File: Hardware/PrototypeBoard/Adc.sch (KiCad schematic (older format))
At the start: 25 parts

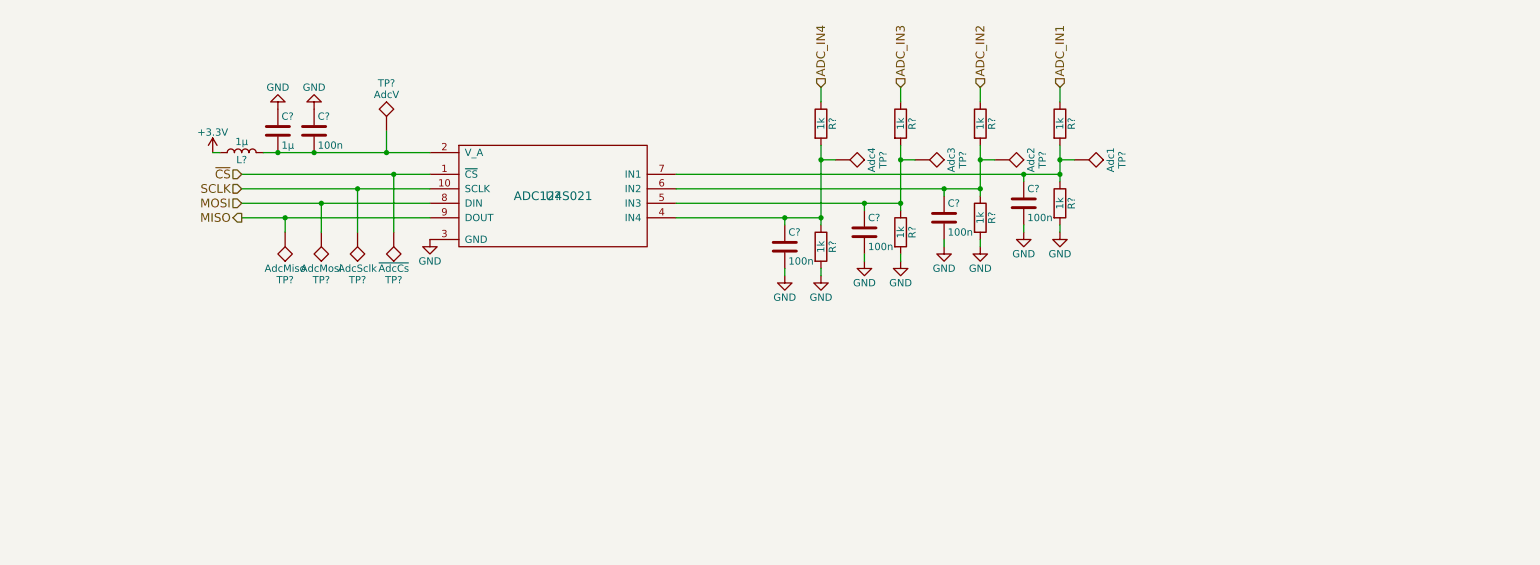
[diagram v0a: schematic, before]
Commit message: Fixed all ERC errors. Added power consumption estimation and other comments. Added links to datasheets. Dimensioned low pass and voltage dividers. Added TVS diodes for protection of voltage rails and ADC inputs. Added fuses. Added Testpoints. Added DC-link capacitors.
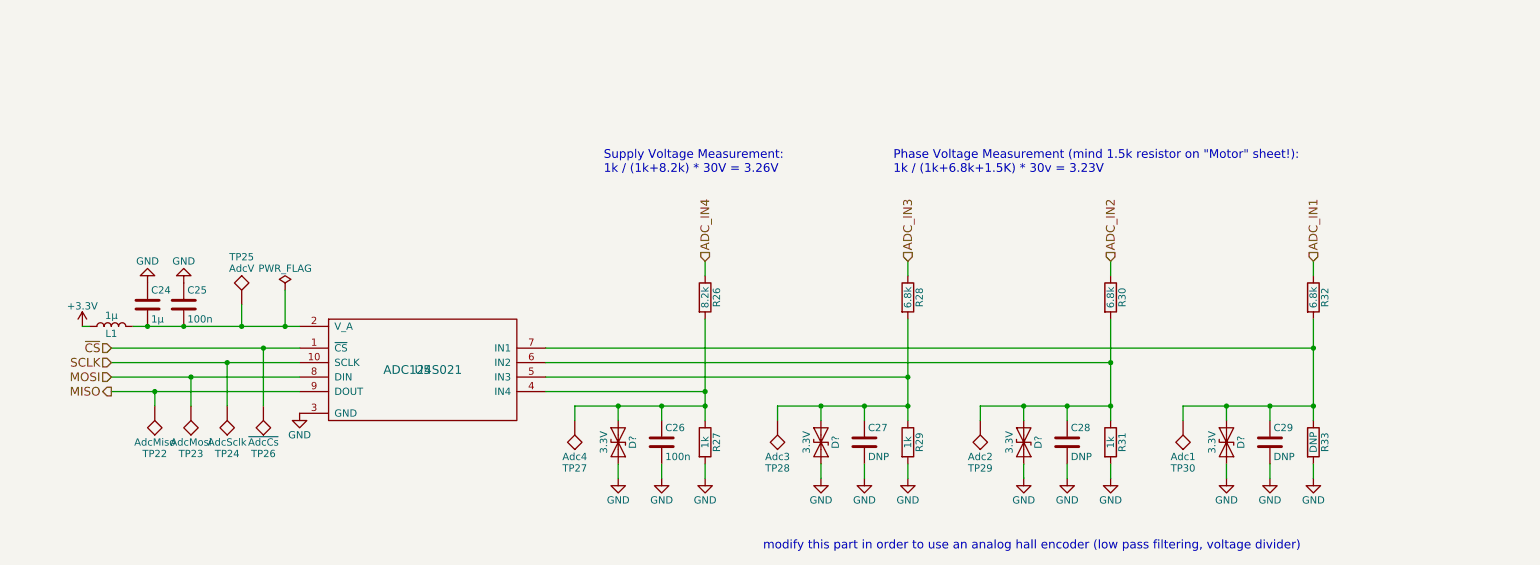
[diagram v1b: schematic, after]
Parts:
- added D? (x4): 3.3V, symbol D_TVS
- C27, C28, C29: renamed from C?; value 100n -> DNP
- R26: renamed from R?; value 1k -> 8.2k
- R28, R30, R32: renamed from R?; value 1k -> 6.8k
- R33: renamed from R?; value 1k -> DNP
- gave numbers to parts that had none: 17
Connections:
- net GND: now also D?.2 (A2), D?.2 (A2), D?.2 (A2), D?.2 (A2)
- net at C26.1, R26.2, R27.1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: now also D?.1 (A1)
- net at C27.1, R28.2, R29.1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: now also D?.1 (A1)
- net at C28.1, R30.2, R31.1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: now also D?.1 (A1)
- net at C29.1, R32.2, R33.1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: now also D?.1 (A1)
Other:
- note added: "Phase Voltage Measurement (mind 1.5k resistor on "Motor" sheet!):\n1k / (1k+6.8k+1.5K) * 30v = 3.23V"
- note added: "Supply Voltage Measurement:\n1k / (1k+8.2k) * 30V = 3.26V"
- note added: "modify this part in order to use an analog hall encoder (low pass filtering, voltage divider)"
- moved on the sheet: C24, C25, C26, C27, C28, C29, L1, R26, R27, R28, R29, R30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

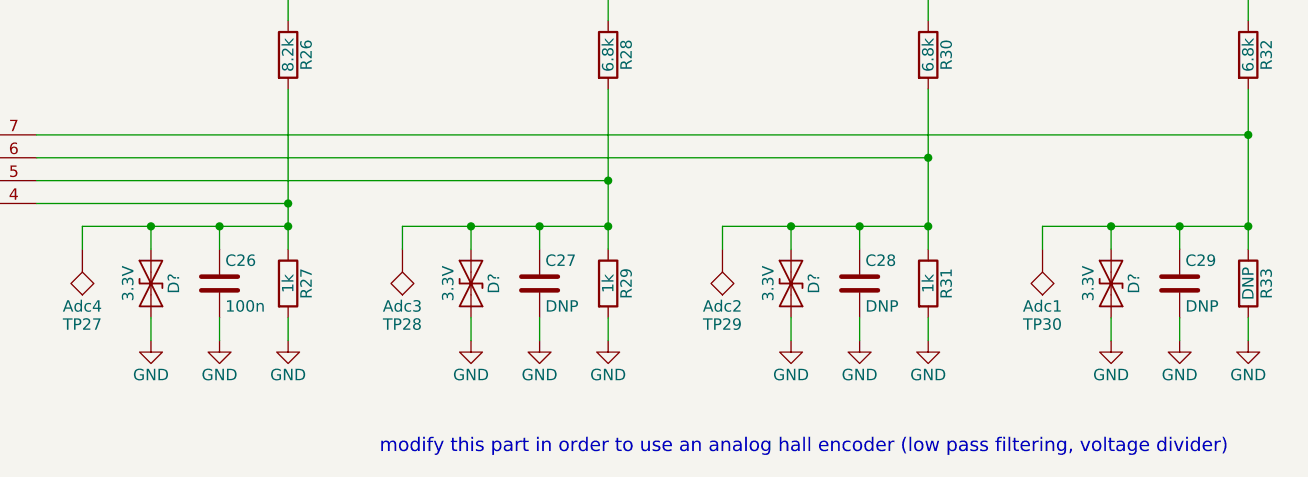
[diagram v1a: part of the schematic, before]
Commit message: Assigned footprints (some of them might still be incorrect). Added relative path to footprints. Generated Netlist.
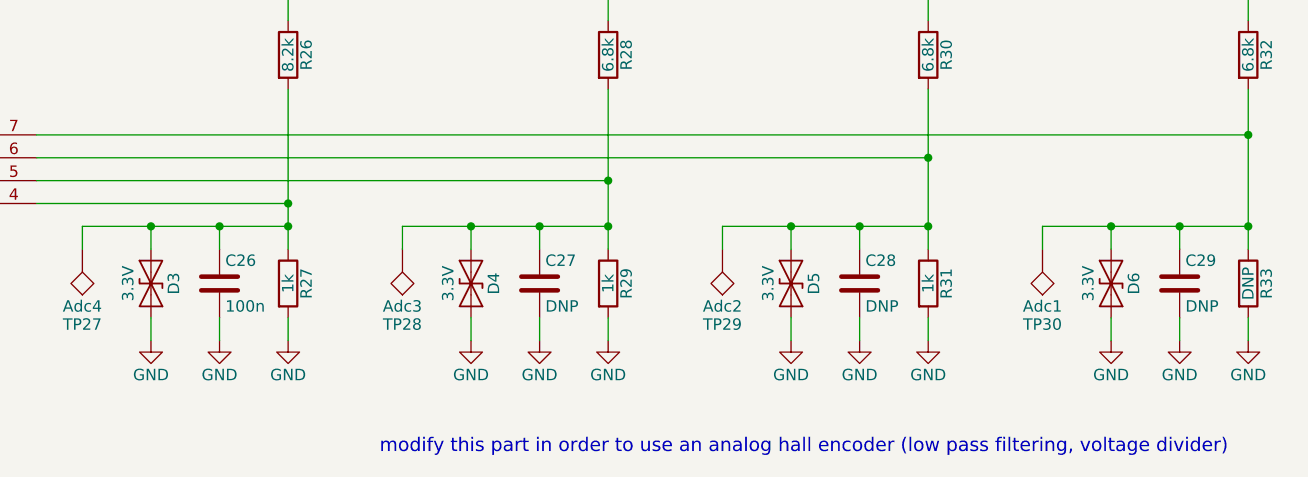
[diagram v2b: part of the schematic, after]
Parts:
- C24, C25, C26, C27, C28, C29: footprint (none) -> Capacitors_SMD:C_0805_HandSoldering
- D3, D4, D5, D6: renamed from D?; footprint (none) -> Diodes_SMD:D_SOD-323_HandSoldering
- L1: footprint (none) -> Inductors_SMD:L_0805_HandSoldering
- R26, R27, R28, R29, R30, R31, R32, R33: footprint (none) -> Resistors_SMD:R_0805_HandSoldering
- TP22, TP23, TP24, TP25, TP26, TP27, TP28, TP29, TP30: footprint (none) -> Measurement_Points:Measurement_Point_Round-TH_Big
- U5: footprint (none) -> libs:ADC124S021CIMMXNOPB
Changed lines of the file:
@@
 F 0 "U5" H 4050 3550 60  0000 C CNN
 F 1 "ADC124S021" H 4050 3550 60  0000 C CNN
-F 2 "" H 4050 3550 60  0001 C CNN
+F 2 "libs:ADC124S021CIMMXNOPB" H 4050 3550 60  0001 C CNN
 F 3 "" H 4050 3550 60  0001 C CNN
 	1    4050 3550
@@
 F 0 "L1" V 1850 3250 50  0000 C CNN
 F 1 "1μ" V 1975 3250 50  0000 C CNN
-F 2 "" H 1900 3250 50  0001 C CNN
+F 2 "Inductors_SMD:L_0805_HandSoldering" H 1900 3250 50  0001 C CNN
 F 3 "" H 1900 3250 50  0001 C CNN
 	1    1900 3250
@@
 F 0 "C25" H 2425 3200 50  0000 L CNN
 F 1 "100n" H 2425 3000 50  0000 L CNN
-F 2 "" H 2438 2950 50  0001 C CNN
+F 2 "Capacitors_SMD:C_0805_HandSoldering" H 2438 2950 50  0001 C CNN
 F 3 "" H 2400 3100 50  0001 C CNN
 	1    2400 3100
@@
 F 0 "C24" H 2175 3200 50  0000 L CNN
 F 1 "1μ" H 2175 3000 50  0000 L CNN
-F 2 "" H 2188 2950 50  0001 C CNN
+F 2 "Capacitors_SMD:C_0805_HandSoldering" H 2188 2950 50  0001 C CNN
 F 3 "" H 2150 3100 50  0001 C CNN
 	1    2150 3100
@@
 F 0 "C29" H 9925 4150 50  0000 L CNN
 F 1 "DNP" H 9925 3950 50  0000 L CNN
-F 2 "" H 9938 3900 50  0001 C CNN
+F 2 "Capacitors_SMD:C_0805_HandSoldering" H 9938 3900 50  0001 C CNN
 F 3 "" H 9900 4050 50  0001 C CNN
 	1    9900 4050
@@
 F 0 "C28" H 8525 4150 50  0000 L CNN
 F 1 "DNP" H 8525 3950 50  0000 L CNN
-F 2 "" H 8538 3900 50  0001 C CNN
+F 2 "Capacitors_SMD:C_0805_HandSoldering" H 8538 3900 50  0001 C CNN
 F 3 "" H 8500 4050 50  0001 C CNN
 	1    8500 4050
@@
 F 0 "C27" H 7125 4150 50  0000 L CNN
 F 1 "DNP" H 7125 3950 50  0000 L CNN
-F 2 "" H 7138 3900 50  0001 C CNN
+F 2 "Capacitors_SMD:C_0805_HandSoldering" H 7138 3900 50  0001 C CNN
 F 3 "" H 7100 4050 50  0001 C CNN
 	1    7100 4050
@@
 F 0 "C26" H 5725 4150 50  0000 L CNN
 F 1 "100n" H 5725 3950 50  0000 L CNN
-F 2 "" H 5738 3900 50  0001 C CNN
+F 2 "Capacitors_SMD:C_0805_HandSoldering" H 5738 3900 50  0001 C CNN
 F 3 "" H 5700 4050 50  0001 C CNN
 	1    5700 4050
@@
 F 0 "R26" V 6080 3050 50  0000 C CNN
 F 1 "8.2k" V 6000 3050 50  0000 C CNN
-F 2 "" V 5930 3050 50  0001 C CNN
+F 2 "Resistors_SMD:R_0805_HandSoldering" V 5930 3050 50  0001 C CNN
 F 3 "" H 6000 3050 50  0001 C CNN
 	1    6000 3050
@@
 F 0 "R28" V 7480 3050 50  0000 C CNN
 F 1 "6.8k" V 7400 3050 50  0000 C CNN
-F 2 "" V 7330 3050 50  0001 C CNN
+F 2 "Resistors_SMD:R_0805_HandSoldering" V 7330 3050 50  0001 C CNN
 F 3 "" H 7400 3050 50  0001 C CNN
 	1    7400 3050
@@
 F 0 "R30" V 8880 3050 50  0000 C CNN
 F 1 "6.8k" V 8800 3050 50  0000 C CNN
-F 2 "" V 8730 3050 50  0001 C CNN
+F 2 "Resistors_SMD:R_0805_HandSoldering" V 8730 3050 50  0001 C CNN
 F 3 "" H 8800 3050 50  0001 C CNN
 	1    8800 3050
@@
 F 0 "R32" V 10280 3050 50  0000 C CNN
 F 1 "6.8k" V 10200 3050 50  0000 C CNN
-F 2 "" V 10130 3050 50  0001 C CNN
+F 2 "Resistors_SMD:R_0805_HandSoldering" V 10130 3050 50  0001 C CNN
 F 3 "" H 10200 3050 50  0001 C CNN
 	1    10200 3050
@@
 F 0 "R33" V 10280 4050 50  0000 C CNN
 F 1 "DNP" V 10200 4050 50  0000 C CNN
-F 2 "" V 10130 4050 50  0001 C CNN
+F 2 "Resistors_SMD:R_0805_HandSoldering" V 10130 4050 50  0001 C CNN
 F 3 "" H 10200 4050 50  0001 C CNN
 	1    10200 4050
@@
 F 0 "R31" V 8880 4050 50  0000 C CNN
 F 1 "1k" V 8800 4050 50  0000 C CNN
-F 2 "" V 8730 4050 50  0001 C CNN
+F 2 "Resistors_SMD:R_0805_HandSoldering" V 8730 4050 50  0001 C CNN
 F 3 "" H 8800 4050 50  0001 C CNN
 	1    8800 4050
@@
 F 0 "R29" V 7480 4050 50  0000 C CNN
 F 1 "1k" V 7400 4050 50  0000 C CNN
-F 2 "" V 7330 4050 50  0001 C CNN
+F 2 "Resistors_SMD:R_0805_HandSoldering" V 7330 4050 50  0001 C CNN
 F 3 "" H 7400 4050 50  0001 C CNN
 	1    7400 4050
@@
 F 0 "R27" V 6080 4050 50  0000 C CNN
 F 1 "1k" V 6000 4050 50  0000 C CNN
-F 2 "" V 5930 4050 50  0001 C CNN
+F 2 "Resistors_SMD:R_0805_HandSoldering" V 5930 4050 50  0001 C CNN
 F 3 "" H 6000 4050 50  0001 C CNN
 	1    6000 4050
@@
 F 0 "TP27" H 5100 4200 50  0000 C BNN
 F 1 "Adc4" H 5100 4150 50  0000 C CNN
-F 2 "" H 5100 3900 50  0001 C CNN
+F 2 "Measurement_Points:Measurement_Point_Round-TH_Big" H 5100 3900 50  0001 C CNN
 F 3 "" H 5100 3900 50  0001 C CNN
 	1    5100 3900
@@
 F 0 "TP28" H 6500 4200 50  0000 C BNN
 F 1 "Adc3" H 6500 4150 50  0000 C CNN
-F 2 "" H 6500 3900 50  0001 C CNN
+F 2 "Measurement_Points:Measurement_Point_Round-TH_Big" H 6500 3900 50  0001 C CNN
 F 3 "" H 6500 3900 50  0001 C CNN
 	1    6500 3900
@@
 F 0 "TP29" H 7900 4200 50  0000 C BNN
 F 1 "Adc2" H 7900 4150 50  0000 C CNN
-F 2 "" H 7900 3900 50  0001 C CNN
+F 2 "Measurement_Points:Measurement_Point_Round-TH_Big" H 7900 3900 50  0001 C CNN
 F 3 "" H 7900 3900 50  0001 C CNN
 	1    7900 3900
@@
 F 0 "TP30" H 9300 4200 50  0000 C BNN
 F 1 "Adc1" H 9300 4150 50  0000 C CNN
-F 2 "" H 9300 3900 50  0001 C CNN
+F 2 "Measurement_Points:Measurement_Point_Round-TH_Big" H 9300 3900 50  0001 C CNN
 F 3 "" H 9300 3900 50  0001 C CNN
 	1    9300 3900
@@
 F 0 "TP25" H 2800 3400 50  0000 C BNN
 F 1 "AdcV" H 2800 3350 50  0000 C CNN
-F 2 "" H 2800 3100 50  0001 C CNN
+F 2 "Measurement_Points:Measurement_Point_Round-TH_Big" H 2800 3100 50  0001 C CNN
 F 3 "" H 2800 3100 50  0001 C CNN
 	1    2800 3100
@@
 F 0 "TP26" H 2950 4100 50  0000 C BNN
 F 1 "~AdcCs" H 2950 4050 50  0000 C CNN
-F 2 "" H 2950 3800 50  0001 C CNN
+F 2 "Measurement_Points:Measurement_Point_Round-TH_Big" H 2950 3800 50  0001 C CNN
 F 3 "" H 2950 3800 50  0001 C CNN
 	1    2950 3800
@@
 F 0 "TP24" H 2700 4100 50  0000 C BNN
 F 1 "AdcSclk" H 2700 4050 50  0000 C CNN
-F 2 "" H 2700 3800 50  0001 C CNN
+F 2 "Measurement_Points:Measurement_Point_Round-TH_Big" H 2700 3800 50  0001 C CNN
 F 3 "" H 2700 3800 50  0001 C CNN
 	1    2700 3800
@@
 F 0 "TP23" H 2450 4100 50  0000 C BNN
 F 1 "AdcMosi" H 2450 4050 50  0000 C CNN
-F 2 "" H 2450 3800 50  0001 C CNN
+F 2 "Measurement_Points:Measurement_Point_Round-TH_Big" H 2450 3800 50  0001 C CNN
 F 3 "" H 2450 3800 50  0001 C CNN
 	1    2450 3800
@@
 F 0 "TP22" H 2200 4100 50  0000 C BNN
 F 1 "AdcMiso" H 2200 4050 50  0000 C CNN
-F 2 "" H 2200 3800 50  0001 C CNN
+F 2 "Measurement_Points:Measurement_Point_Round-TH_Big" H 2200 3800 50  0001 C CNN
 F 3 "" H 2200 3800 50  0001 C CNN
 	1    2200 3800
@@
 modify this part in order to use an analog hall encoder (low pass filtering, voltage divider)
 $Comp
-L D_TVS D?
+L D_TVS D6
 U 1 1 5AFF1E54
 P 9600 4050
-F 0 "D?" H 9600 4150 50  0000 C CNN
+F 0 "D6" H 9600 4150 50  0000 C CNN
 F 1 "3.3V" H 9600 3950 50  0000 C CNN
-F 2 "" H 9600 4050 50  0001 C CNN
+F 2 "Diodes_SMD:D_SOD-323_HandSoldering" H 9600 4050 50  0001 C CNN
 F 3 "" H 9600 4050 50  0001 C CNN
 	1    9600 4050
@@
 $EndComp
 $Comp
-L D_TVS D?
+L D_TVS D3
 U 1 1 5AFF1F87
 P 5400 4050
-F 0 "D?" H 5400 4150 50  0000 C CNN
+F 0 "D3" H 5400 4150 50  0000 C CNN
 F 1 "3.3V" H 5400 3950 50  0000 C CNN
-F 2 "" H 5400 4050 50  0001 C CNN
+F 2 "Diodes_SMD:D_SOD-323_HandSoldering" H 5400 4050 50  0001 C CNN
 F 3 "" H 5400 4050 50  0001 C CNN
 	1    5400 4050
@@
 $EndComp
 $Comp
-L D_TVS D?
+L D_TVS D4
 U 1 1 5AFF2000
 P 6800 4050
-F 0 "D?" H 6800 4150 50  0000 C CNN
+F 0 "D4" H 6800 4150 50  0000 C CNN
 F 1 "3.3V" H 6800 3950 50  0000 C CNN
-F 2 "" H 6800 4050 50  0001 C CNN
+F 2 "Diodes_SMD:D_SOD-323_HandSoldering" H 6800 4050 50  0001 C CNN
 F 3 "" H 6800 4050 50  0001 C CNN
 	1    6800 4050
@@
 $EndComp
 $Comp
-L D_TVS D?
+L D_TVS D5
 U 1 1 5AFF208E
 P 8200 4050
-F 0 "D?" H 8200 4150 50  0000 C CNN
+F 0 "D5" H 8200 4150 50  0000 C CNN
 F 1 "3.3V" H 8200 3950 50  0000 C CNN
-F 2 "" H 8200 4050 50  0001 C CNN
+F 2 "Diodes_SMD:D_SOD-323_HandSoldering" H 8200 4050 50  0001 C CNN
 F 3 "" H 8200 4050 50  0001 C CNN
 	1    8200 4050

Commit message: minor progress in layout
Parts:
- TP22, TP23, TP24, TP25, TP26, TP27, TP28, TP29, TP30: footprint Measurement_Points:Measurement_Point_Round-TH_Big -> Measurement_Points:Measurement_Point_Round-SMD-Pad_Small
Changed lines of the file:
@@
 F 0 "TP27" H 5100 4200 50  0000 C BNN
 F 1 "Adc4" H 5100 4150 50  0000 C CNN
-F 2 "Measurement_Points:Measurement_Point_Round-TH_Big" H 5100 3900 50  0001 C CNN
+F 2 "Measurement_Points:Measurement_Point_Round-SMD-Pad_Small" H 5100 3900 50  0001 C CNN
 F 3 "" H 5100 3900 50  0001 C CNN
 	1    5100 3900
@@
 F 0 "TP28" H 6500 4200 50  0000 C BNN
 F 1 "Adc3" H 6500 4150 50  0000 C CNN
-F 2 "Measurement_Points:Measurement_Point_Round-TH_Big" H 6500 3900 50  0001 C CNN
+F 2 "Measurement_Points:Measurement_Point_Round-SMD-Pad_Small" H 6500 3900 50  0001 C CNN
 F 3 "" H 6500 3900 50  0001 C CNN
 	1    6500 3900
@@
 F 0 "TP29" H 7900 4200 50  0000 C BNN
 F 1 "Adc2" H 7900 4150 50  0000 C CNN
-F 2 "Measurement_Points:Measurement_Point_Round-TH_Big" H 7900 3900 50  0001 C CNN
+F 2 "Measurement_Points:Measurement_Point_Round-SMD-Pad_Small" H 7900 3900 50  0001 C CNN
 F 3 "" H 7900 3900 50  0001 C CNN
 	1    7900 3900
@@
 F 0 "TP30" H 9300 4200 50  0000 C BNN
 F 1 "Adc1" H 9300 4150 50  0000 C CNN
-F 2 "Measurement_Points:Measurement_Point_Round-TH_Big" H 9300 3900 50  0001 C CNN
+F 2 "Measurement_Points:Measurement_Point_Round-SMD-Pad_Small" H 9300 3900 50  0001 C CNN
 F 3 "" H 9300 3900 50  0001 C CNN
 	1    9300 3900
@@
 F 0 "TP25" H 2800 3400 50  0000 C BNN
 F 1 "AdcV" H 2800 3350 50  0000 C CNN
-F 2 "Measurement_Points:Measurement_Point_Round-TH_Big" H 2800 3100 50  0001 C CNN
+F 2 "Measurement_Points:Measurement_Point_Round-SMD-Pad_Small" H 2800 3100 50  0001 C CNN
 F 3 "" H 2800 3100 50  0001 C CNN
 	1    2800 3100
@@
 F 0 "TP26" H 2950 4100 50  0000 C BNN
 F 1 "~AdcCs" H 2950 4050 50  0000 C CNN
-F 2 "Measurement_Points:Measurement_Point_Round-TH_Big" H 2950 3800 50  0001 C CNN
+F 2 "Measurement_Points:Measurement_Point_Round-SMD-Pad_Small" H 2950 3800 50  0001 C CNN
 F 3 "" H 2950 3800 50  0001 C CNN
 	1    2950 3800
@@
 F 0 "TP24" H 2700 4100 50  0000 C BNN
 F 1 "AdcSclk" H 2700 4050 50  0000 C CNN
-F 2 "Measurement_Points:Measurement_Point_Round-TH_Big" H 2700 3800 50  0001 C CNN
+F 2 "Measurement_Points:Measurement_Point_Round-SMD-Pad_Small" H 2700 3800 50  0001 C CNN
 F 3 "" H 2700 3800 50  0001 C CNN
 	1    2700 3800
@@
 F 0 "TP23" H 2450 4100 50  0000 C BNN
 F 1 "AdcMosi" H 2450 4050 50  0000 C CNN
-F 2 "Measurement_Points:Measurement_Point_Round-TH_Big" H 2450 3800 50  0001 C CNN
+F 2 "Measurement_Points:Measurement_Point_Round-SMD-Pad_Small" H 2450 3800 50  0001 C CNN
 F 3 "" H 2450 3800 50  0001 C CNN
 	1    2450 3800
@@
 F 0 "TP22" H 2200 4100 50  0000 C BNN
 F 1 "AdcMiso" H 2200 4050 50  0000 C CNN
-F 2 "Measurement_Points:Measurement_Point_Round-TH_Big" H 2200 3800 50  0001 C CNN
+F 2 "Measurement_Points:Measurement_Point_Round-SMD-Pad_Small" H 2200 3800 50  0001 C CNN
 F 3 "" H 2200 3800 50  0001 C CNN
 	1    2200 3800
